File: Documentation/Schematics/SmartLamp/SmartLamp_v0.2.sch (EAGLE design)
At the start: 18 parts, among them IC1 DS3231/SO, U1 HM-10

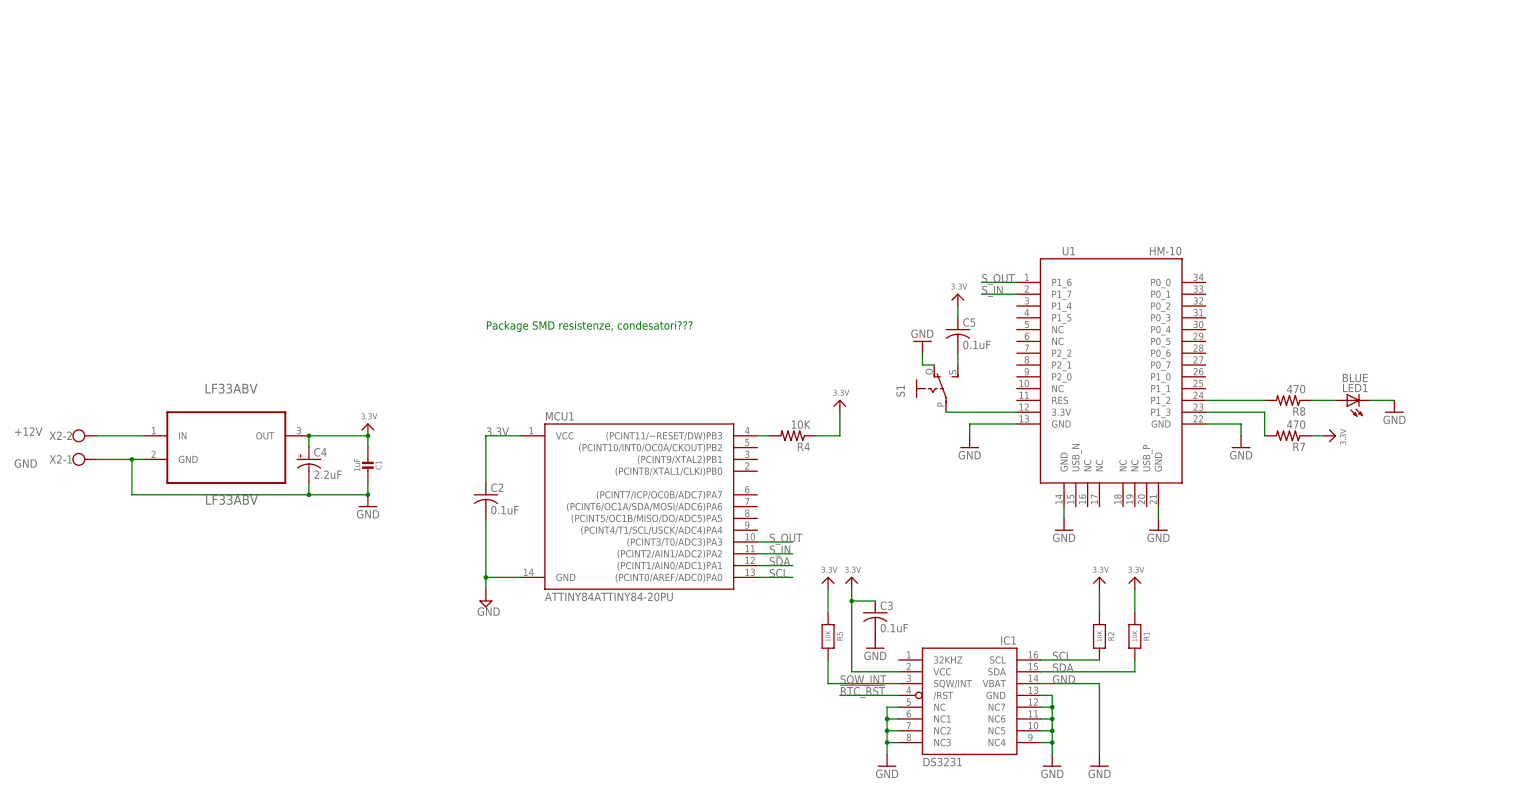
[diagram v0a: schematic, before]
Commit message: Complete first version of schematic and board. Added first partlist and BOM
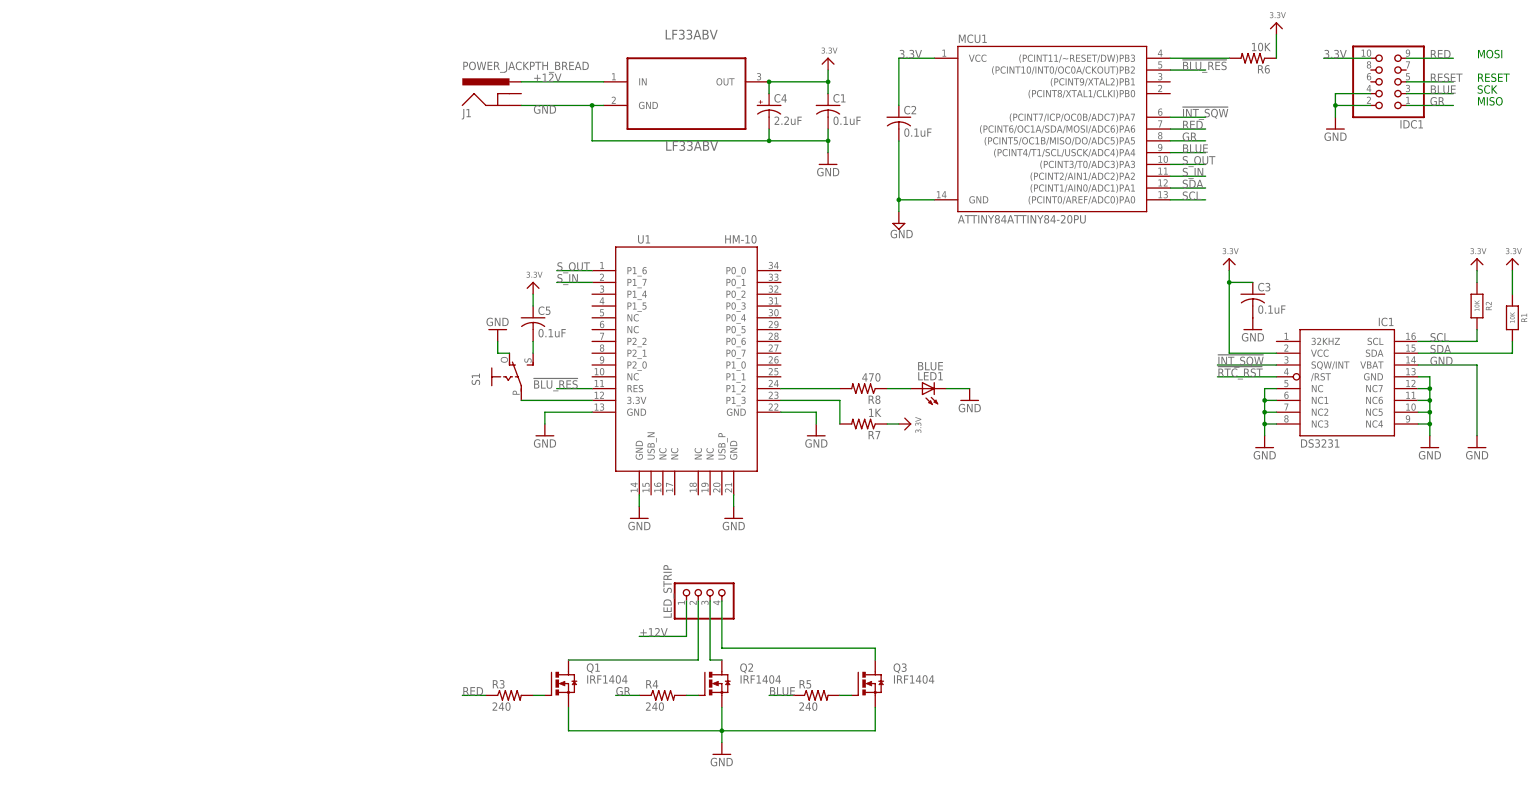
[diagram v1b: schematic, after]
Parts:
- removed X2: (no value), con-wago-500:W237-102
- added IDC1: (no value), pinhead:PINHD-2X5
- added J1: POWER_JACKPTH_BREAD, SparkFun-Connectors:POWER_JACKPTH_BREAD
- added LED_STRIP: (no value), pinhead:PINHD-1X4
- added Q1, Q2, Q3: IRF1404, transistor-power:IRFI540NPBF
- added R3: 240, rcl:R-US_0207/10
- added R6: 10K, rcl:R-US_0207/10
- C1: value 1uF -> 0.1uF; device microbuilder:CAP_CERAMIC0805-NOOUTLINE -> adafruit:C-US025-024X044
- C3: device adafruit:C-USC0805 -> adafruit:C-US025-024X044
- R4: value 10K -> 240
- R5: value 10K -> 240; device microbuilder:RESISTOR0805_NOOUTLINE -> rcl:R-US_0207/10
- R7: value 470 -> 1K
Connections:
- removed net N$5: MCU1.(PCINT11/~RESET/DW)PB3, R4.2
- removed net SQW_INT: IC1.SQW/INT, R5.2
- new net !BLU_RES: MCU1.(PCINT10/INT0/OC0A/CKOUT)PB2, U1.RES
- new net !INT_SQW: IC1.SQW/INT, MCU1.(PCINT7/ICP/OC0B/ADC7)PA7
- new net BLUE: IDC1.3, MCU1.(PCINT4/T1/SCL/USCK/ADC4)PA4, R5.1
- new net GR: IDC1.1, MCU1.(PCINT5/OC1B/MISO/DO/ADC5)PA5, R4.1
- new net N$11: Q3.G, R5.2
- new net N$3: LED_STRIP.2, Q1.D
- new net N$4: LED_STRIP.3, Q2.D
- new net N$6: LED_STRIP.4, Q3.D
- new net N$7: Q1.G, R3.2
- new net N$8: Q2.G, R4.2
- new net RED: IDC1.9, MCU1.(PCINT6/OC1A/SDA/MOSI/ADC6)PA6, R3.1
- new net RESET: IDC1.5, MCU1.(PCINT11/~RESET/DW)PB3, R6.2
- net +12V: now also J1.PWR, LED_STRIP.1; no longer X2-2.KL
- net 3.3V: now also C1.1, IDC1.10, R6.1; no longer C1.2, R4.1, R5.1
- net GND: now also C1.2, IDC1.2, IDC1.4, J1.GND, Q1.S, Q2.S, Q3.S; no longer C1.1, X2-1.KL
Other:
- note added: "MISO"
- note added: "MOSI"
- note added: "RESET"
- note added: "SCK"
- note removed: "Package SMD resistenze, condesatori???"
- moved on the sheet: C1, C2, C3, C4, C5, IC1, LED1, LF33ABV, MCU1, R1, R2, R4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
